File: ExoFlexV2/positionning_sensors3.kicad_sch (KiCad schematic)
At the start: 27 parts

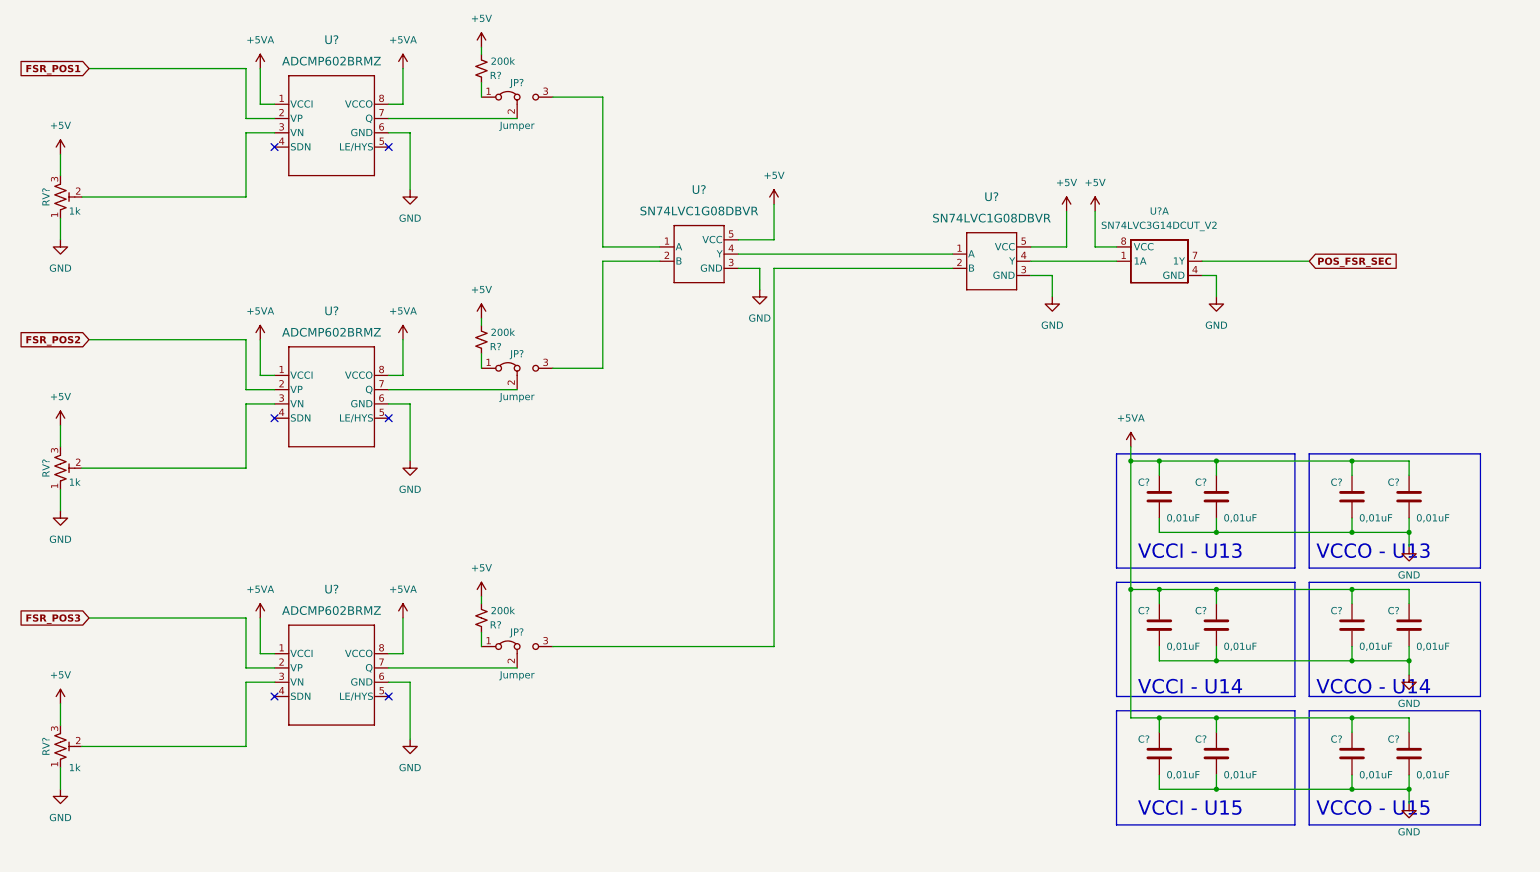
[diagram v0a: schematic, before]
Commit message: Mise à jour signaux STM
- Condo de découplage
- Signaux supplémentaire pour le STM
- Page GND sera pour Multiplexeur
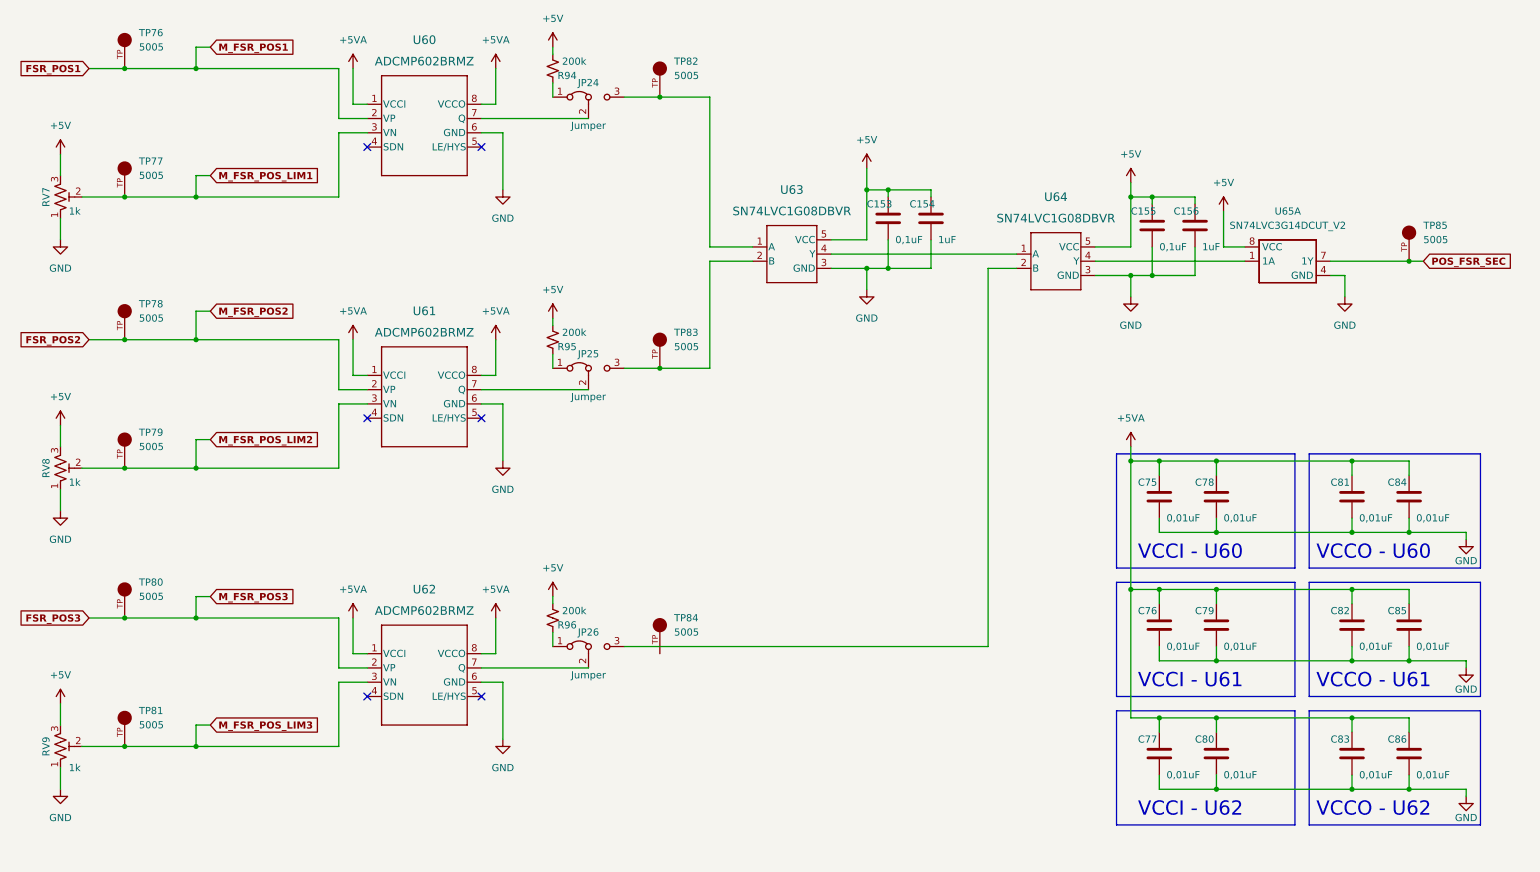
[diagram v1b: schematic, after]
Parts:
- added C153, C155: 0,1uF, Capacitor_SMD:C_0603_1608Metric, symbol Device:C
- added C154, C156: 1uF, Capacitor_SMD:C_0603_1608Metric, symbol Device:C
- added TP76, TP77, TP78, TP79, TP80, TP81, TP82, TP83, TP84, TP85: 5005, FootPrint:KEYSTONE_5005, symbol SymLib:5005
- gave numbers to parts that had none: 27
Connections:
- net +5V: now also C153.1, C154.1, C155.1, C156.1
- net FSR_POS1: now also TP76.TP
- net FSR_POS2: now also TP78.TP
- net FSR_POS3: now also TP80.TP
- net GND: now also C153.2, C154.2, C155.2, C156.2
- net POS_FSR_SEC: now also TP85.TP
- net M_FSR_POS_LIM3: now reaches RV9.2, U62.3 (VN)
- net M_FSR_POS_LIM3: now also TP81.TP
- net at JP25.3 (B), U63.2 (B): now also TP83.TP
- net at JP24.3 (B), U63.1 (A): now also TP82.TP
- net M_FSR_POS_LIM2: now reaches RV8.2, U61.3 (VN)
- net M_FSR_POS_LIM2: now also TP79.TP
- net M_FSR_POS_LIM1: now reaches RV7.2, U60.3 (VN)
- net M_FSR_POS_LIM1: now also TP77.TP
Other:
- note added: "VCCI - U60"
- note added: "VCCI - U61"
- note added: "VCCI - U62"
- note added: "VCCO - U60"
- note added: "VCCO - U61"
- note added: "VCCO - U62"
- note removed: "VCCI - U13"
- note removed: "VCCI - U14"
- note removed: "VCCI - U15"
- note removed: "VCCO - U13"
- note removed: "VCCO - U14"
- note removed: "VCCO - U15"
- moved on the sheet: JP24, JP25, JP26, R94, R95, R96, U60, U61, U62, U63, U64, U65A

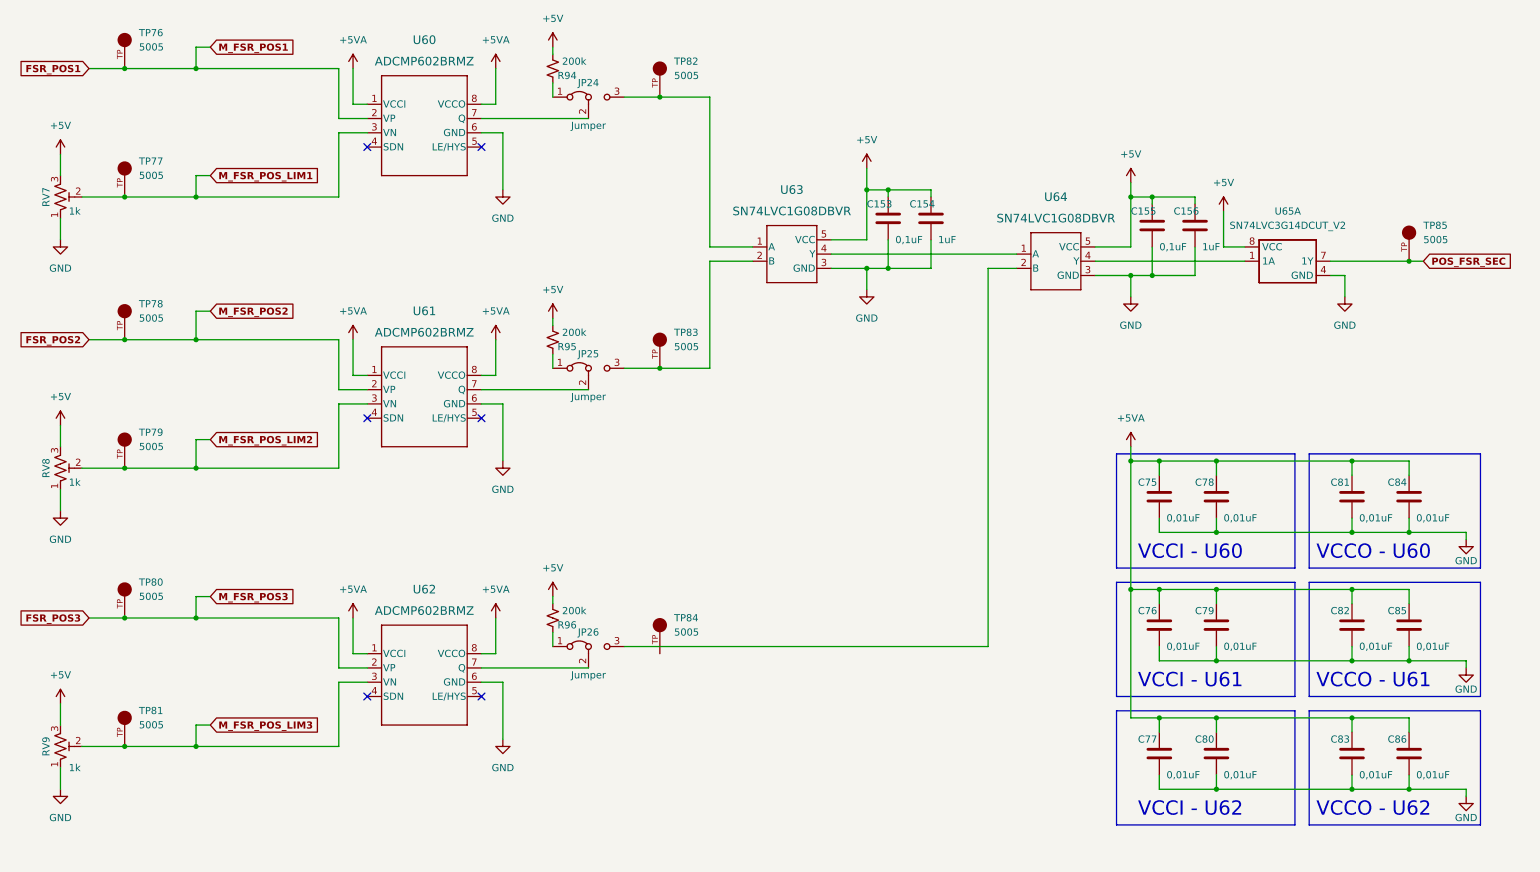
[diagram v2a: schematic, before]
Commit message: Finalisation 1
- Ajout de pages pour la gestion des signaux négatif
- Modification des pages de torque et amplitude
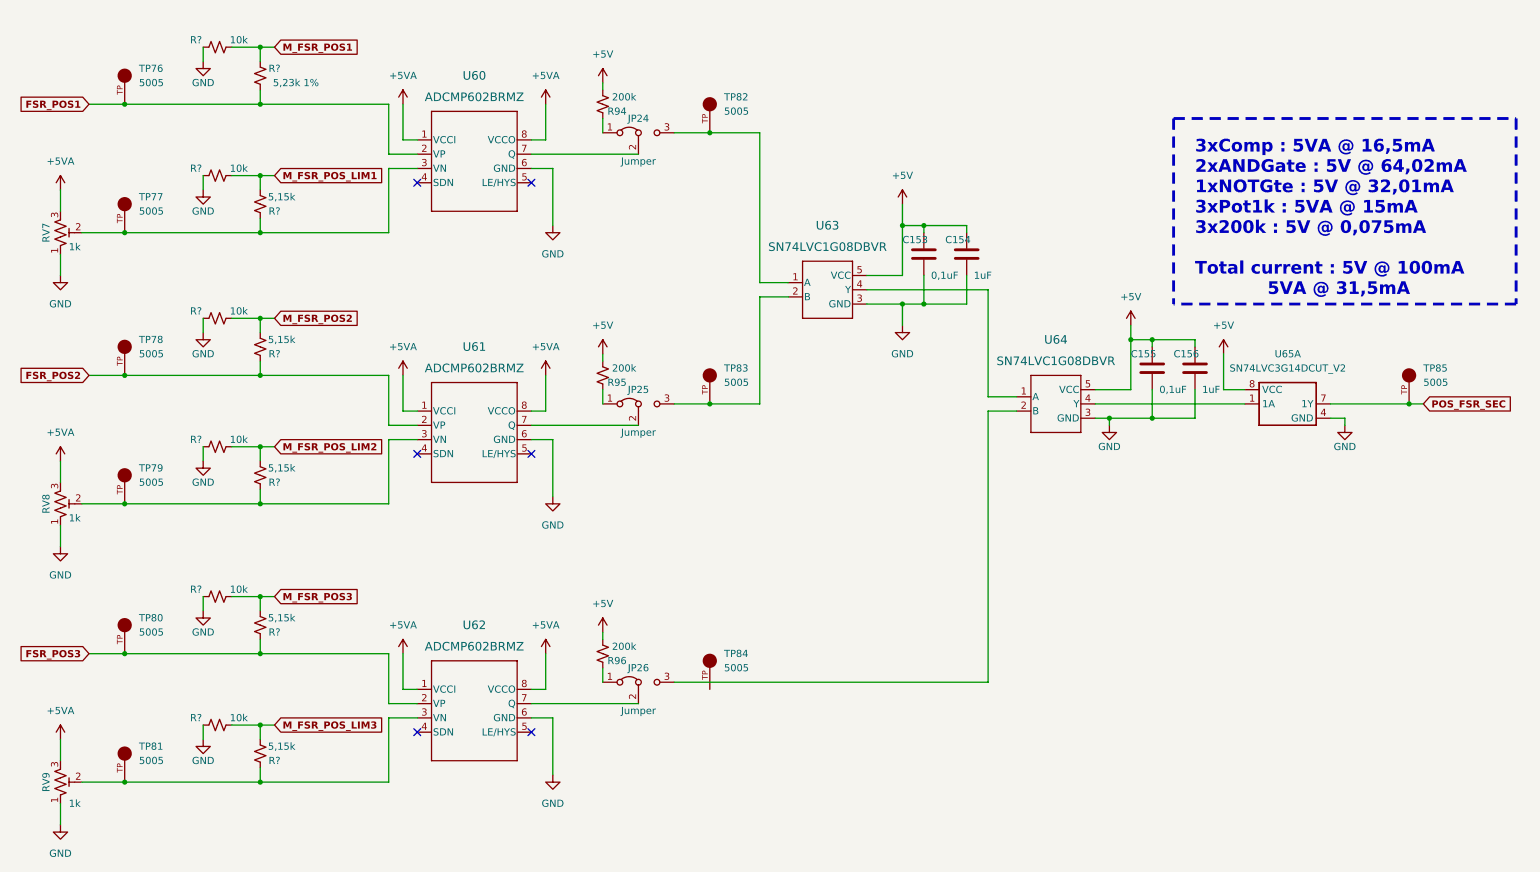
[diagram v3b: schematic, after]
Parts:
- removed C75, C76, C77, C78, C79, C80, C81, C82, C83, C84, C85, C86: 0,01uF, Capacitor_SMD:C_0603_1608Metric, symbol Device:C
- added R? (x5): 5,15k, Resistor_SMD:R_0805_2012Metric, symbol Device:R_Small_US
- added R? (x6): 10k, Resistor_SMD:R_0805_2012Metric, symbol Device:R_Small_US
- added R?: 5,23k 1%, Resistor_SMD:R_0805_2012Metric, symbol Device:R_Small_US
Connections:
- net +5V: no longer RV7.3, RV8.3, RV9.3
- net +5VA: now also RV7.3, RV8.3, RV9.3
- net FSR_POS1: now also R?.2
- net FSR_POS2: now also R?.2
- net FSR_POS3: now also R?.2
- net GND: now also R?.1, R?.1, R?.1, R?.1, R?.1, R?.1
- net M_FSR_POS_LIM1: now also R?.1, R?.2; no longer RV7.2, TP77.TP, U60.3 (VN)
- net M_FSR_POS_LIM2: now also R?.1, R?.2; no longer RV8.2, TP79.TP, U61.3 (VN)
- net M_FSR_POS_LIM3: now also R?.1, R?.2; no longer RV9.2, TP81.TP, U62.3 (VN)
- new net: R?.2, RV9.2, TP81.TP, U62.3 (VN)
- new net: R?.2, RV8.2, TP79.TP, U61.3 (VN)
- new net: R?.2, RV7.2, TP77.TP, U60.3 (VN)
- new net M_FSR_POS1: R?.1, R?.2
- new net M_FSR_POS2: R?.1, R?.2
- new net M_FSR_POS3: R?.1, R?.2
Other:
- note added: "3xComp : 5VA @ 16,5mA 2xANDGate : 5V @ 64,02mA 1xNOTGte : 5V @ 32,01mA 3xPot1k : 5VA @ 15mA 3x200k : 5V @ 0,075mA Total current : 5V @ 100mA 5VA @ 31,5mA"
- note removed: "VCCI - U60"
- note removed: "VCCI - U61"
- note removed: "VCCI - U62"
- note removed: "VCCO - U60"
- note removed: "VCCO - U61"
- note removed: "VCCO - U62"
- moved on the sheet: C153, C154, C155, C156, JP24, JP25, JP26, R94, R95, R96, RV7, RV8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
